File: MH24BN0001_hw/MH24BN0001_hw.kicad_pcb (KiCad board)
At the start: 2 copper layers, 1 part, among them J1 ST-Link V2 Header

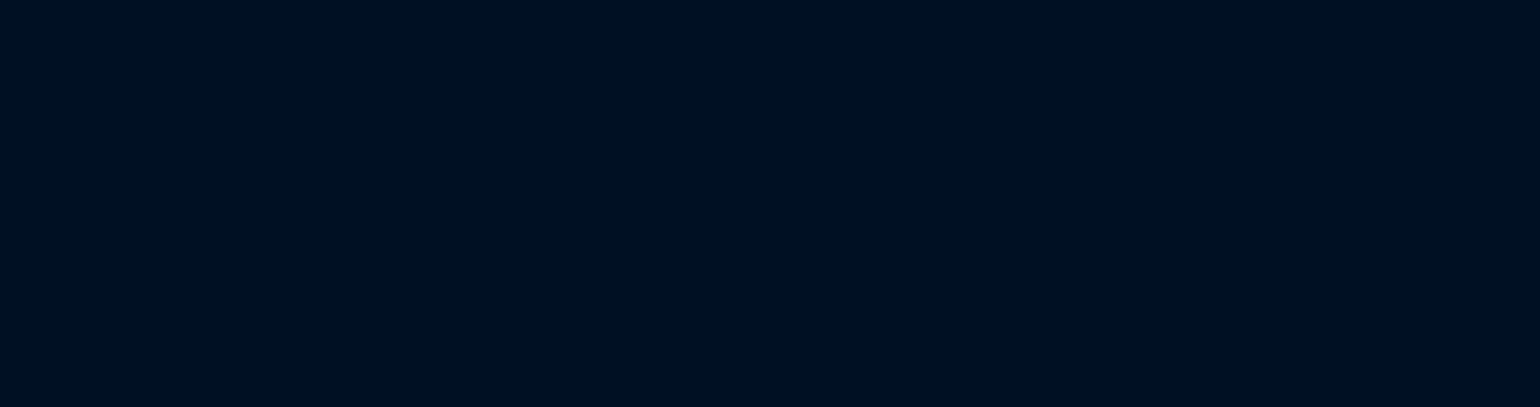
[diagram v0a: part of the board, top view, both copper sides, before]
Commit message: Adding serial interface to board, finishing schematic
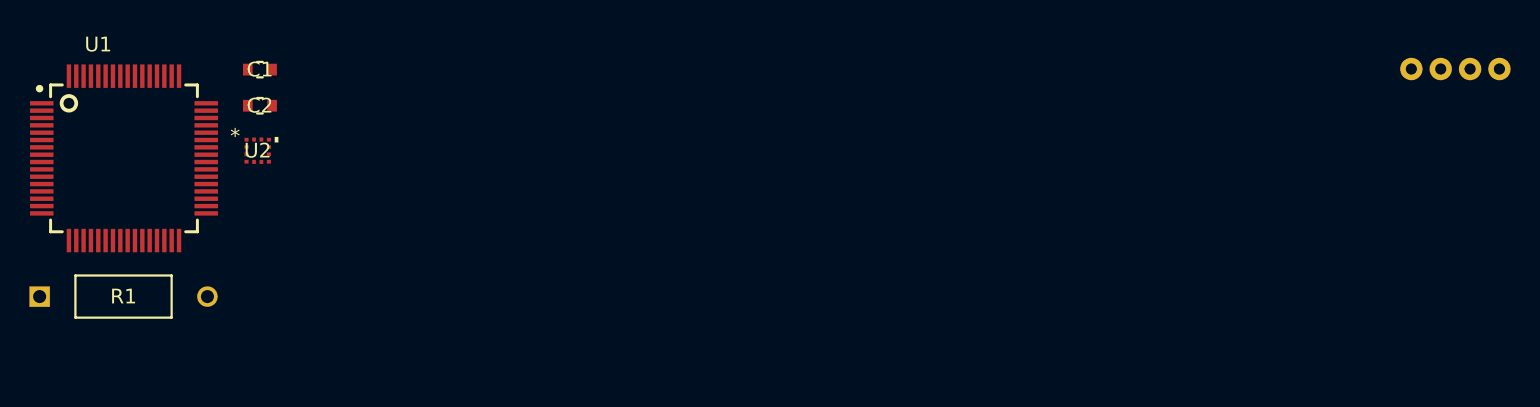
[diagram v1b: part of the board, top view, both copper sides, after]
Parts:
- added C1: 1µF, Library:1µF_cap, F.Cu at (68.6, 40.0)
- added C2: 2.2µF, Library:2.2µF_cap, F.Cu at (68.6, 42.5)
- added R1: 10 kΩ, Library:10 kΩ, F.Cu at (53.6, 55.5)
- added SI1: ~, Library:serial_interface, F.Cu at (150.0, 40.0)
- added U1: STM32F401RBT6, Library:QFP50P1200X1200X160-64N, F.Cu at (59.3, 46.1)
- added U2: Accelerometer, Library:acc, F.Cu at (68.4, 45.6)
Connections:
- J1 pad 1: unconnected-(J1-Pad1) -> +3.3V
- J1 pad 10: unconnected-(J1-Pad10) -> GND
- J1 pad 12: unconnected-(J1-Pad12) -> GND
- J1 pad 14: unconnected-(J1-Pad14) -> GND
- J1 pad 15: unconnected-(J1-Pad15) -> /NRST
- J1 pad 16: unconnected-(J1-Pad16) -> GND
- J1 pad 18: unconnected-(J1-Pad18) -> GND
- J1 pad 2: unconnected-(J1-Pad2) -> +3.3V
- J1 pad 20: unconnected-(J1-Pad20) -> GND
- J1 pad 3: unconnected-(J1-Pad3) -> GND
- J1 pad 4: unconnected-(J1-Pad4) -> GND
- J1 pad 5: unconnected-(J1-Pad5) -> GND
- J1 pad 6: unconnected-(J1-Pad6) -> GND
- J1 pad 7: unconnected-(J1-Pad7) -> /SWDIO
- J1 pad 8: unconnected-(J1-Pad8) -> GND
- J1 pad 9: unconnected-(J1-Pad9) -> /SWCLK

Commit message: starting PCB
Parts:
- moved J1 126.2 mm to (33.2, 43.2), turned to 90 degrees
- moved SI1 60.7 mm to (89.5, 44.5)
- moved R1 26.6 mm to (47.8, 29.5)
- moved U1 8.82 mm to (51.5, 42.0)
- moved C1 5.54 mm to (70.8, 35.0)
- moved C2 5.54 mm to (70.8, 37.4)
- moved U2 5.54 mm to (70.6, 40.5)
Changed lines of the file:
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@@
 	(footprint "Library:QFP50P1200X1200X160-64N"
 		(layer "F.Cu")
-		(at 59.3163 46.0867)
+		(at 51.5 42)
 		(property "Reference" "U1"
 			(at -1.757345 -7.750405 0)
@@
 		)
 		(property "Value" "STM32F401RBT6"
-			(at 9.120105 7.672755 0)
+			(at 0 10 0)
 			(layer "F.Fab")
 			(effects
@@
 	(footprint "Library:61302021821"
 		(layer "F.Cu")
-		(at 149.77 91.73 -90)
+		(at 33.23 43.19 90)
 		(descr "<B>WR-PHD </B><BR> 2.54 mm Dual Socket Header,20 Pins")
 		(property "Reference" "J1"
-			(at -15.73 -0.23 180)
+			(at 14.19 -0.23 0)
 			(layer "F.SilkS")
 			(effects
@@
 		)
 		(property "Value" "ST-Link V2 Header"
-			(at -14.23 -0.23 180)
+			(at -14.23 -0.23 360)
 			(layer "F.Fab")
 			(effects
@@
 		)
 		(property "ROWS" "Dual"
-			(at 0 0 -90)
+			(at 0 0 90)
 			(unlocked yes)
 			(layer "F.Fab")
@@
 		)
 		(property "GENDER" "Socket Header"
-			(at 0 0 -90)
+			(at 0 0 90)
 			(unlocked yes)
 			(layer "F.Fab")
@@
 		)
 		(property "MOUNT" "THT"
-			(at 0 0 -90)
+			(at 0 0 90)
 			(unlocked yes)
 			(layer "F.Fab")
@@
 		)
 		(property "IR" "3A"
-			(at 0 0 -90)
+			(at 0 0 90)
 			(unlocked yes)
 			(layer "F.Fab")
@@
 		)
 		(property "VALUE" "61302021821"
-			(at 0 0 -90)
+			(at 0 0 90)
 			(unlocked yes)
 			(layer "F.Fab")
@@
 		)
 		(property "PACKAGING" "Tray"
-			(at 0 0 -90)
+			(at 0 0 90)
 			(unlocked yes)
 			(layer "F.Fab")
@@
 		)
 		(property "PART-NUMBER" "61302021821"
-			(at 0 0 -90)
+			(at 0 0 90)
 			(unlocked yes)
 			(layer "F.Fab")
@@
 		)
 		(property "DATASHEET-URL" "https://www.we-online.com/redexpert/spec/61302021821?ae"
-			(at 0 0 -90)
+			(at 0 0 90)
 			(unlocked yes)
 			(layer "F.Fab")
@@
 		)
 		(property "PITCH" "2.54mm"
-			(at 0 0 -90)
+			(at 0 0 90)
 			(unlocked yes)
 			(layer "F.Fab")
@@
 		)
 		(property "PINS" "20"
-			(at 0 0 -90)
+			(at 0 0 90)
 			(unlocked yes)
 			(layer "F.Fab")
@@
 		)
 		(property "TYPE" "Straight"
-			(at 0 0 -90)
+			(at 0 0 90)
 			(unlocked yes)
 			(layer "F.Fab")
@@
 		(attr through_hole)
 		(fp_line
-			(start -13.05 2.64)
-			(end -13.05 -2.64)
+			(start 13.05 -2.64)
+			(end 13.05 2.64)
 			(stroke
 				(width 0.2)
@@
 		)
 		(fp_line
-			(start 13.05 2.64)
-			(end -13.05 2.64)
+			(start -13.05 -2.64)
+			(end 13.05 -2.64)
 			(stroke
 				(width 0.2)
@@
 		)
 		(fp_line
-			(start -13.05 -2.64)
-			(end 13.05 -2.64)
+			(start 13.05 2.64)
+			(end -13.05 2.64)
 			(stroke
 				(width 0.2)
@@
 		)
 		(fp_line
-			(start 13.05 -2.64)
-			(end 13.05 2.64)
+			(start -13.05 2.64)
+			(end -13.05 -2.64)
 			(stroke
 				(width 0.2)
@@
 		)
 		(fp_line
-			(start -12.95 2.54)
-			(end 12.95 2.54)
+			(start 12.95 -2.54)
+			(end -12.95 -2.54)
 			(stroke
 				(width 0.1)
@@
 		)
 		(fp_line
-			(start 12.95 2.54)
-			(end 12.95 -2.54)
+			(start -12.95 -2.54)
+			(end -12.95 2.54)
 			(stroke
 				(width 0.1)
@@
 		)
 		(fp_line
-			(start -12.95 -2.54)
-			(end -12.95 2.54)
+			(start 12.95 2.54)
+			(end 12.95 -2.54)
 			(stroke
 				(width 0.1)
@@
 		)
 		(fp_line
-			(start 12.95 -2.54)
-			(end -12.95 -2.54)
+			(start -12.95 2.54)
+			(end 12.95 2.54)
 			(stroke
 				(width 0.1)
@@
 		)
 		(pad "1" thru_hole circle
-			(at -11.43 1.27 270)
+			(at -11.43 1.27 90)
 			(size 1.53 1.53)
 			(drill 1.02)
@@
 		)
 		(pad "2" thru_hole circle
-			(at -11.43 -1.27 270)
+			(at -11.43 -1.27 90)
 			(size 1.53 1.53)
 			(drill 1.02)
@@
 		)
 		(pad "3" thru_hole circle
-			(at -8.89 1.27 270)
+			(at -8.89 1.27 90)
 			(size 1.53 1.53)
 			(drill 1.02)
@@
 		)
 		(pad "4" thru_hole circle
-			(at -8.89 -1.27 270)
+			(at -8.89 -1.27 90)
 			(size 1.53 1.53)
 			(drill 1.02)
@@
 		)
 		(pad "5" thru_hole circle
-			(at -6.35 1.27 270)
+			(at -6.35 1.27 90)
 			(size 1.53 1.53)
 			(drill 1.02)
@@
 		)
 		(pad "6" thru_hole circle
-			(at -6.35 -1.27 270)
+			(at -6.35 -1.27 90)
 			(size 1.53 1.53)
 			(drill 1.02)
@@
 		)
 		(pad "7" thru_hole circle
-			(at -3.81 1.27 270)
+			(at -3.81 1.27 90)
 			(size 1.53 1.53)
 			(drill 1.02)
@@
 		)
 		(pad "8" thru_hole circle
-			(at -3.81 -1.27 270)
+			(at -3.81 -1.27 90)
 			(size 1.53 1.53)
 			(drill 1.02)
@@
 		)
 		(pad "9" thru_hole circle
-			(at -1.27 1.27 270)
+			(at -1.27 1.27 90)
 			(size 1.53 1.53)
 			(drill 1.02)
@@
 		)
 		(pad "10" thru_hole circle
-			(at -1.27 -1.27 270)
+			(at -1.27 -1.27 90)
 			(size 1.53 1.53)
 			(drill 1.02)
@@
 		)
 		(pad "11" thru_hole circle
-			(at 1.27 1.27 270)
+			(at 1.27 1.27 90)
 			(size 1.53 1.53)
 			(drill 1.02)
@@
 		)
 		(pad "12" thru_hole circle
-			(at 1.27 -1.27 270)
+			(at 1.27 -1.27 90)
 			(size 1.53 1.53)
 			(drill 1.02)
@@
 		)
 		(pad "13" thru_hole circle
-			(at 3.81 1.27 270)
+			(at 3.81 1.27 90)
 			(size 1.53 1.53)
 			(drill 1.02)
@@
 		)
 		(pad "14" thru_hole circle
-			(at 3.81 -1.27 270)
+			(at 3.81 -1.27 90)
 			(size 1.53 1.53)
 			(drill 1.02)
@@
 		)
 		(pad "15" thru_hole circle
-			(at 6.35 1.27 270)
+			(at 6.35 1.27 90)
 			(size 1.53 1.53)
 			(drill 1.02)
@@
 		)
 		(pad "16" thru_hole circle
-			(at 6.35 -1.27 270)
+			(at 6.35 -1.27 90)
 			(size 1.53 1.53)
 			(drill 1.02)
@@
 		)
 		(pad "17" thru_hole circle
-			(at 8.89 1.27 270)
+			(at 8.89 1.27 90)
 			(size 1.53 1.53)
 			(drill 1.02)
@@
 		)
 		(pad "18" thru_hole circle
-			(at 8.89 -1.27 270)
+			(at 8.89 -1.27 90)
 			(size 1.53 1.53)
 			(drill 1.02)
@@
 		)
 		(pad "19" thru_hole circle
-			(at 11.43 1.27 270)
+			(at 11.43 1.27 90)
 			(size 1.53 1.53)
 			(drill 1.02)
@@
 		)
 		(pad "20" thru_hole circle
-			(at 11.43 -1.27 270)
+			(at 11.43 -1.27 90)
 			(size 1.53 1.53)
 			(drill 1.02)
@@
 	(footprint "Library:2.2µF_cap"
 		(layer "F.Cu")
-		(at 68.5771 42.5023)
+		(at 70.7608 37.4156)
 		(tags "CL10A225KO8NNNC ")
 		(property "Reference" "C2"
@@
 			(polygon
 				(pts
-					(xy 68.1279 42.1531) (xy 69.0263 42.1531) (xy 69.0263 42.8515) (xy 68.1279 42.8515)
+					(xy 70.3116 37.0664) (xy 71.21 37.0664) (xy 71.21 37.7648) (xy 70.3116 37.7648)
 				)
 			)
@@
 	(footprint "Library:10 kΩ"
 		(layer "F.Cu")
-		(at 53.57 55.5)
+		(at 47.785 29.5)
 		(tags "CF14JT10K0 ")
 		(property "Reference" "R1"
@@
 		)
 		(property "Footprint" "Library:10 kΩ"
-			(at 0 0 0)
+			(at 0 0 360)
 			(layer "F.Fab")
 			(hide yes)
@@
 		)
 		(property "Datasheet" "https://www.digikey.com/en/products/detail/stackpole-electronics-inc/CF14JT10K0/1741265"
-			(at 0 0 0)
+			(at 0 0 360)
 			(layer "F.Fab")
 			(hide yes)
@@
 		)
 		(property "Description" ""
-			(at 0 0 0)
+			(at 0 0 360)
 			(layer "F.Fab")
 			(hide yes)
@@
 	(footprint "Library:1µF_cap"
 		(layer "F.Cu")
-		(at 68.5771 40.0419)
+		(at 70.7608 34.9552)
 		(tags "CL10B105KP8NNNC ")
 		(property "Reference" "C1"
@@
 			(polygon
 				(pts
-					(xy 68.1279 39.6927) (xy 69.0263 39.6927) (xy 69.0263 40.3911) (xy 68.1279 40.3911)
+					(xy 70.3116 34.606) (xy 71.21 34.606) (xy 71.21 35.3044) (xy 70.3116 35.3044)
 				)
 			)
@@
 	(footprint "Library:serial_interface"
 		(layer "F.Cu")
-		(at 150 40)
+		(at 89.5 44.5)
 		(property "Reference" "SI1"
 			(at 0 -4 0)
@@
 	(footprint "Library:acc"
 		(layer "F.Cu")
-		(at 68.4248 45.5652)
+		(at 70.6085 40.4785)
 		(tags "LIS2DTW12TR ")
 		(property "Reference" "U2"
@@
 		)
 	)
+	(gr_rect
+		(start 26.5 25.5)
+		(end 126.5 60.5)
+		(stroke
+			(width 0.2)
+			(type default)
+		)
+		(fill none)
+		(layer "F.Cu")
+		(net 3)
+	)
 )

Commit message: finishing pcb, generating output files
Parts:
- added C1: 1µF, Library:1µF_cap, F.Cu at (49.0, 50.0)
- added C2: 1µF, Library:1µF_cap, F.Cu at (56.5, 50.0)
- added C4: 1µF, Library:1µF_cap, F.Cu at (47.5, 34.5)
- added C5: 1µF, Library:1µF_cap, F.Cu at (43.5, 44.0)
- added C6: 1µF, Library:1µF_cap, F.Cu at (42.8, 37.5)
- moved C7 21.8 mm to (53.0, 50.0)
- moved SI1 20.8 mm to (69.0, 48.0), turned to -90 degrees
- moved U2 18.0 mm to (54.0, 33.5), turned to 180 degrees
- moved C3 11.5 mm to (60.0, 39.0), turned to -90 degrees
- moved R1 6.00 mm to (41.8, 29.5)
- renumbered C1 to C3, C2 to C7
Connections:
- C7 pad 1: Net-(U1-VCAP1) -> +3.3V
- U1 pad 30: Net-(U1-VCAP1) -> +3.3V
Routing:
- net GND: track 0.00 -> 188.7 mm, vias 0 -> 3
- net +3.3V: track 0.00 -> 156.9 mm, vias 0 -> 3
- net /SWDIO: track 0.00 -> 34.0 mm, vias 0 -> 2
- net /SWCLK: track 0.00 -> 31.6 mm, vias 0 -> 2
- net /MCU_TX: track 0.00 -> 15.1 mm
- net /MCU_RX: track 0.00 -> 14.5 mm
- net /NRST: track 0.00 -> 13.2 mm
- net /SDA: track 0.00 -> 9.29 mm
- net Net-(U1-BOOT0): track 0.00 -> 7.84 mm
- net /SCL: track 0.00 -> 5.80 mm
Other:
- board outline added: 47 x 34.5 mm

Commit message: Generating new and final output files by which I ordered the PCB
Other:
- board text added: "MH24BN0001"
